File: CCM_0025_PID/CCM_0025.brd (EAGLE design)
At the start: 41.9 x 69.8 mm, 110 parts, among them IC1 AD825, IC10 AD825, IC11 AD825, IC2 AD825, IC3 AD8226, IC4 AD8226, IC5 AD825, IC6 AD825, IC7 AD825, IC8 AD825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

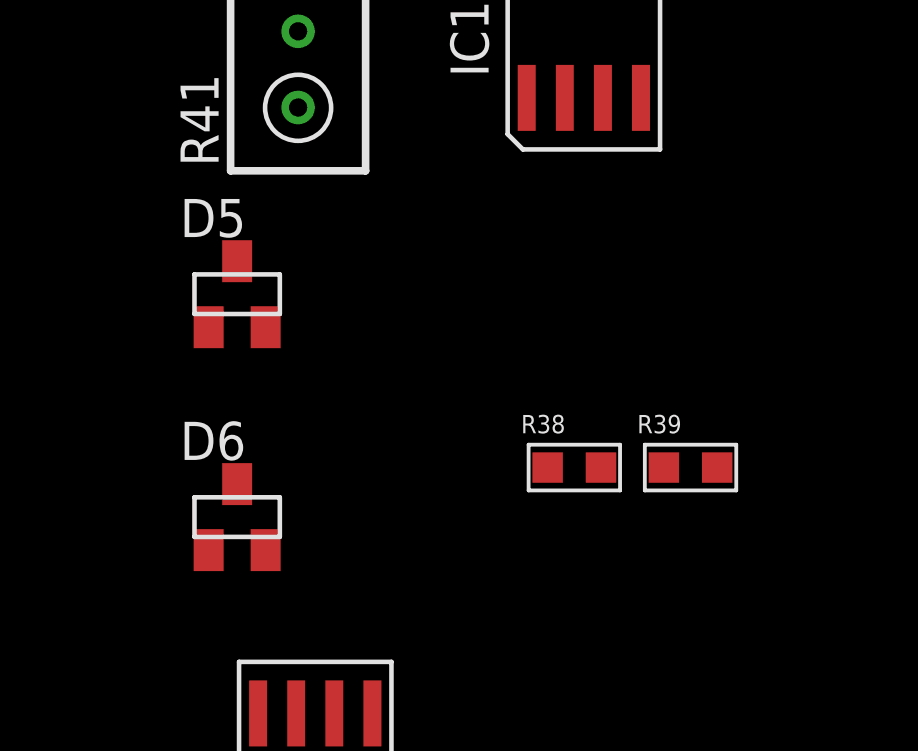
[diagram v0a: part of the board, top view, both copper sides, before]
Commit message: updates to schematic of CCM_0025, PID
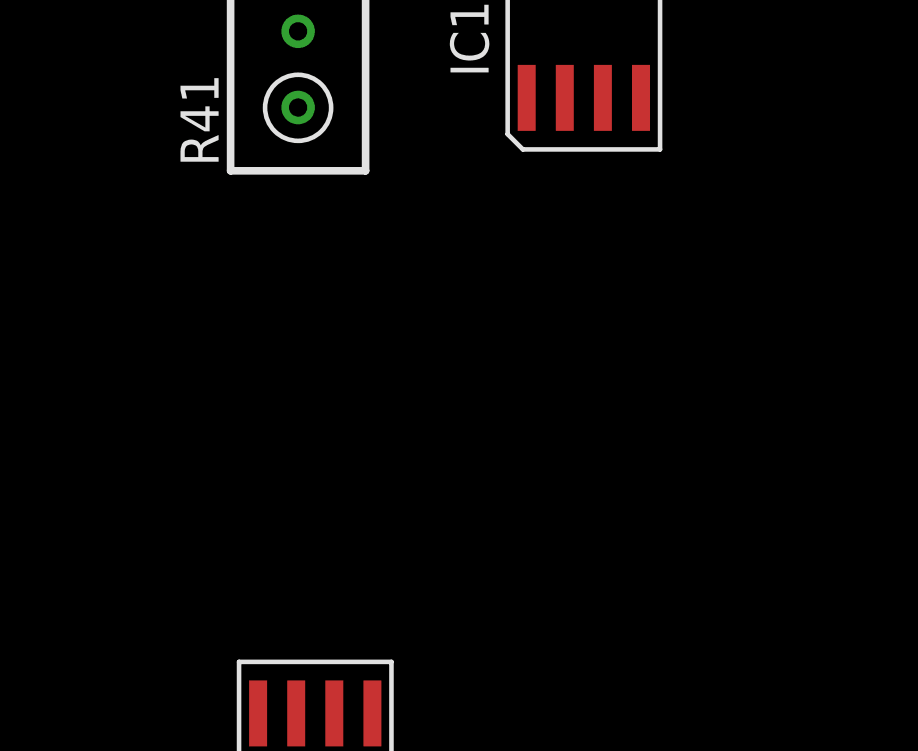
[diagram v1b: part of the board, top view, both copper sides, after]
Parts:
- removed D5, D6: LM4040-10V, noah:SOT23
- removed R38, R39: 10k, acrooptics:0603
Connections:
- removed net N$22: D3.1, R36.1, R40.1
- removed net N$28: D3.2, D4.1
- removed net N$35: D5.1, R38.1, R41.1
- removed net N$40: D4.2, R37.2, R40.3
- removed net N$42: D5.2, D6.1
- removed net N$43: D6.2, R39.2, R41.3
- new net +10V: D3.1, R36.1, R40.1, R41.1
- new net -10V: D4.2, R37.2, R40.3, R41.3
- net GND: now also D3.2, D4.1
- net V+: no longer R38.2
- net V-: no longer R39.1
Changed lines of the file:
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@@
 <attribute name="VALUE" x="-123.317" y="-194.183" size="0.6096" layer="27" font="vector" ratio="20"/>
-</element>
-<element name="R38" library="acrooptics" package="0603" value="10k" x="-110.2995" y="-214.0585" smashed="yes">
-<attribute name="NAME" x="-112.0775" y="-212.9155" size="0.6096" layer="25" font="vector" ratio="20"/>
-<attribute name="VALUE" x="-111.9505" y="-215.8365" size="0.6096" layer="27" font="vector" ratio="20"/>
-</element>
-<element name="R39" library="acrooptics" package="0603" value="10k" x="-106.426" y="-214.0585" smashed="yes">
-<attribute name="NAME" x="-108.204" y="-212.9155" size="0.6096" layer="25" font="vector" ratio="20"/>
-<attribute name="VALUE" x="-108.077" y="-215.8365" size="0.6096" layer="27" font="vector" ratio="20"/>
-</element>
-<element name="D5" library="noah" package="SOT23" value="LM4040-10V" x="-121.539" y="-208.28" smashed="yes">
-<attribute name="NAME" x="-123.444" y="-206.375" size="1.27" layer="25"/>
-<attribute name="VALUE" x="-123.444" y="-211.455" size="1.27" layer="27"/>
-</element>
-<element name="D6" library="noah" package="SOT23" value="LM4040-10V" x="-121.539" y="-215.7095" smashed="yes">
-<attribute name="NAME" x="-123.444" y="-213.8045" size="1.27" layer="25"/>
-<attribute name="VALUE" x="-123.444" y="-218.8845" size="1.27" layer="27"/>
 </element>
 <element name="IC11" library="noah" package="SO8" value="AD825" x="-109.982" y="-199.136" smashed="yes">
@@
 <contactref element="C11" pad="2"/>
 <contactref element="C12" pad="1"/>
+<contactref element="D3" pad="2"/>
+<contactref element="D4" pad="1"/>
+<wire x1="-113.5355" y1="-148.42" x2="-111.6355" y2="-140.9905" width="0" layer="19" extent="1-1"/>
+<wire x1="-103.124" y1="-124.0155" x2="-111.6355" y2="-140.9905" width="0" layer="19" extent="1-1"/>
 <wire x1="-92.837" y1="-124.0155" x2="-103.124" y2="-124.0155" width="0" layer="19" extent="1-1"/>
 <wire x1="-90.7415" y1="-124.0155" x2="-92.837" y2="-124.0155" width="0" layer="19" extent="1-1"/>
@@
 <wire x1="-5.08" y1="45.9105" x2="-8.255" y2="44.3865" width="0" layer="19" extent="1-1"/>
 <wire x1="-12.7" y1="44.1325" x2="-8.255" y2="44.3865" width="0" layer="19" extent="1-1"/>
-<wire x1="-118.3005" y1="-227.4535" x2="-103.124" y2="-124.0155" width="0" layer="19" extent="1-1"/>
+<wire x1="-118.3005" y1="-227.4535" x2="-113.5355" y2="-148.42" width="0" layer="19" extent="1-1"/>
 <wire x1="-133.5405" y1="-226.949" x2="-118.3005" y2="-227.4535" width="0" layer="19" extent="1-1"/>
 <wire x1="-139.573" y1="-226.949" x2="-133.5405" y2="-226.949" width="0" layer="19" extent="1-1"/>
@@
 <wire x1="15.24" y1="30.861" x2="13.335" y2="30.861" width="0.4064" layer="1"/>
 <contactref element="IC10" pad="4"/>
-<contactref element="R39" pad="1"/>
 <contactref element="IC11" pad="4"/>
 <contactref element="IC8" pad="4"/>
@@
 <wire x1="-108.077" y1="-159.064" x2="-88.9635" y2="-124.0155" width="0" layer="19" extent="1-1"/>
 <wire x1="-108.077" y1="-201.736" x2="-108.077" y2="-159.064" width="0" layer="19" extent="1-1"/>
-<wire x1="-107.315" y1="-214.0585" x2="-108.077" y2="-201.736" width="0" layer="19" extent="1-1"/>
-<wire x1="-117.0305" y1="-227.4535" x2="-107.315" y2="-214.0585" width="0" layer="19" extent="1-1"/>
+<wire x1="-117.0305" y1="-227.4535" x2="-108.077" y2="-201.736" width="0" layer="19" extent="1-1"/>
 <wire x1="-137.795" y1="-226.949" x2="-117.0305" y2="-227.4535" width="0" layer="19" extent="1-1"/>
 <wire x1="-25.781" y1="-65.592" x2="-72.3265" y2="-100.4535" width="0" layer="19" extent="1-1"/>
@@
 <wire x1="10.795" y1="32.639" x2="7.62" y2="32.639" width="0.4064" layer="1"/>
 <contactref element="IC10" pad="7"/>
-<contactref element="R38" pad="2"/>
 <contactref element="IC11" pad="7"/>
 <contactref element="IC8" pad="7"/>
@@
 <wire x1="-110.617" y1="-153.864" x2="-94.615" y2="-124.0155" width="0" layer="19" extent="1-1"/>
 <wire x1="-110.617" y1="-196.536" x2="-110.617" y2="-153.864" width="0" layer="19" extent="1-1"/>
-<wire x1="-109.4105" y1="-214.0585" x2="-110.617" y2="-196.536" width="0" layer="19" extent="1-1"/>
-<wire x1="-119.5705" y1="-222.2535" x2="-109.4105" y2="-214.0585" width="0" layer="19" extent="1-1"/>
+<wire x1="-119.5705" y1="-222.2535" x2="-110.617" y2="-196.536" width="0" layer="19" extent="1-1"/>
 <wire x1="-135.3185" y1="-226.949" x2="-119.5705" y2="-222.2535" width="0" layer="19" extent="1-1"/>
 <wire x1="-28.321" y1="-60.392" x2="-74.8665" y2="-95.2535" width="0" layer="19" extent="1-1"/>
@@
 <wire x1="22.225" y1="66.04" x2="-105.6005" y2="-124.0155" width="0" layer="19" extent="1-1"/>
 </signal>
-<signal name="N$22">
-<contactref element="R36" pad="1"/>
-<contactref element="D3" pad="1"/>
-<contactref element="R40" pad="1"/>
-<wire x1="-119.507" y1="-158.369" x2="-113.5355" y2="-140.9905" width="0" layer="19" extent="1-1"/>
-<wire x1="-27.051" y1="-46.9265" x2="-113.5355" y2="-140.9905" width="0" layer="19" extent="1-1"/>
-</signal>
-<signal name="N$28">
-<contactref element="D3" pad="2"/>
-<contactref element="D4" pad="1"/>
-<wire x1="-113.5355" y1="-148.42" x2="-111.6355" y2="-140.9905" width="0" layer="19" extent="1-1"/>
-</signal>
-<signal name="N$40">
-<contactref element="D4" pad="2"/>
-<contactref element="R37" pad="2"/>
-<contactref element="R40" pad="3"/>
-<wire x1="-111.6355" y1="-148.42" x2="-29.5275" y2="-46.9265" width="0" layer="19" extent="1-1"/>
-<wire x1="-119.507" y1="-153.289" x2="-111.6355" y2="-148.42" width="0" layer="19" extent="1-1"/>
-</signal>
 <signal name="N$41">
 <contactref element="IC10" pad="3"/>
@@
 <wire x1="-123.043" y1="-178.308" x2="-122.555" y2="-188.0235" width="0" layer="19" extent="1-1"/>
 </signal>
-<signal name="N$35">
-<contactref element="R38" pad="1"/>
-<contactref element="D5" pad="1"/>
-<contactref element="R41" pad="1"/>
-<wire x1="-119.507" y1="-202.057" x2="-122.489" y2="-209.38" width="0" layer="19" extent="1-1"/>
-<wire x1="-111.1885" y1="-214.0585" x2="-122.489" y2="-209.38" width="0" layer="19" extent="1-1"/>
-</signal>
-<signal name="N$42">
-<contactref element="D5" pad="2"/>
-<contactref element="D6" pad="1"/>
-<wire x1="-120.589" y1="-209.38" x2="-122.489" y2="-216.8095" width="0" layer="19" extent="1-1"/>
-</signal>
-<signal name="N$43">
-<contactref element="D6" pad="2"/>
-<contactref element="R39" pad="2"/>
-<contactref element="R41" pad="3"/>
-<wire x1="-105.537" y1="-214.0585" x2="-120.589" y2="-216.8095" width="0" layer="19" extent="1-1"/>
-<wire x1="-119.507" y1="-196.977" x2="-120.589" y2="-216.8095" width="0" layer="19" extent="1-1"/>
-</signal>
 <signal name="N$44">
 <contactref element="IC11" pad="3"/>
@@
 <wire x1="-129.286" y1="-226.949" x2="-118.3005" y2="-222.2535" width="0" layer="19" extent="1-1"/>
 </signal>
+<signal name="+10V">
+<contactref element="R36" pad="1"/>
+<contactref element="D3" pad="1"/>
+<contactref element="R41" pad="1"/>
+<contactref element="R40" pad="1"/>
+<wire x1="-119.507" y1="-158.369" x2="-113.5355" y2="-140.9905" width="0" layer="19" extent="1-1"/>
+<wire x1="-119.507" y1="-202.057" x2="-119.507" y2="-158.369" width="0" layer="19" extent="1-1"/>
+<wire x1="-27.051" y1="-46.9265" x2="-113.5355" y2="-140.9905" width="0" layer="19" extent="1-1"/>
+</signal>
+<signal name="-10V">
+<contactref element="D4" pad="2"/>
+<contactref element="R37" pad="2"/>
+<contactref element="R41" pad="3"/>
+<contactref element="R40" pad="3"/>
+<wire x1="-111.6355" y1="-148.42" x2="-29.5275" y2="-46.9265" width="0" layer="19" extent="1-1"/>
+<wire x1="-119.507" y1="-153.289" x2="-111.6355" y2="-148.42" width="0" layer="19" extent="1-1"/>
+<wire x1="-119.507" y1="-196.977" x2="-119.507" y2="-153.289" width="0" layer="19" extent="1-1"/>
+</signal>
 </signals>
